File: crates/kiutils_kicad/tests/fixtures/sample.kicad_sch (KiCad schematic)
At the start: 1 part

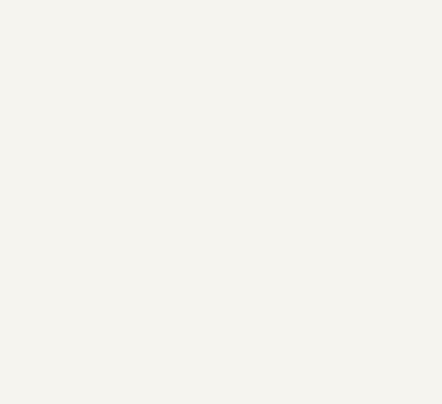
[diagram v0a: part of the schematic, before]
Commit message: feat(kicad): add schematic symbol instance read/write APIs
Add APIs for reading and editing symbol instance properties in KiCad
schematics, supporting BOM workflow use cases (e.g. populating MPN,
Manufacturer fields).

New APIs:
- symbol_instances() — list all symbols with reference, value, footprint,
  lib_id, and all properties
- upsert_symbol_instance_property() — create or update a property on
  symbols matching a reference designator
- remove_symbol_instance_property() — remove a property from matching
  symbols
- sheet_filenames() — list sub-sheet filenames for hierarchical traversal

Co-Authored-By: Claude <noreply@anthropic.com>
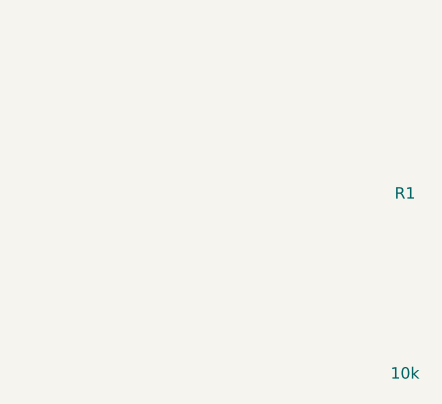
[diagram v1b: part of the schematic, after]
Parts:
- removed ?: (no value), symbol Device:R
- added R1: 10k, Resistor_SMD:R_0603, symbol Device:R
